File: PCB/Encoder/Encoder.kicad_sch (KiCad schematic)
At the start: 19 parts, among them J2 1-1734595-0, J3 Conn_01x06_Pin, U2 DS90LV017ATMX/NOPB, U3 AS5047P-ATSM, U4 DS90LV018ATM, U5 DS90LV018ATM

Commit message: Updated Schematics and PCB
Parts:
- removed C2, C4, C6: 0.001uF, symbol Device:C
- removed C3, C5, C7: 0.1uF, symbol Device:C
- removed C8: 4.7uF, symbol Device:C
- removed FB2, FB3: 600R, FerriteBeadCustom:IND_BOURNS_1005, symbol Device:FerriteBead
- removed J3: Conn_01x06_Pin, symbol Connector:Conn_01x06_Pin
- removed R1, R2: 100R, symbol Device:R
- removed U2: DS90LV017ATMX/NOPB, LVDSCustom:SOIC127P599X175-8N, symbol LVDSCustom:DS90LV017ATMX_NOPB
- removed U4, U5: DS90LV018ATM, DS90LV018ATM:SOIC127P599X175-8N, symbol LVDSCustom:DS90LV018ATM
- added H1, H2, H3, H4: MountingHole, MountingHole:MountingHole_3.2mm_M3, symbol Mechanical:MountingHole
- C1: footprint (none) -> Capacitor_SMD:C_0805_2012Metric
- C2: renamed from C9; footprint (none) -> Capacitor_SMD:C_0805_2012Metric
- J1: renamed from J2; value 1-1734595-0 -> 1-1734595-0 Header; footprint CON10_1X10_DUM_HPI_TYC -> ConnectorCustom:CON10_1X10_DUM_HPI_TYC
- U1: renamed from U3; footprint TSSOP14_OSM -> AngleSensor:TSSOP14_OSM
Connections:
- net CLK_M is gone; now on net I: J1.8
- net CLK_P is gone; now on net B: J1.7
- net MISO_M is gone; now on net A: J1.6
- net MISO_P is gone; now on net MOSI: J1.5
- net MOSI_M is gone; now on net CLK: J1.3
- net MOSI_P is gone; now on net CS_: J1.2
- net +3.3V: now also J1.1
- net CS_: no longer J1.4
- net MISO: now also J1.4
- net I: now reaches U1.14 (I/PWM)
- net A: now reaches U1.6 (B)
- net B: now reaches U1.7 (A)
- no-connect marks 10 -> 4
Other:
- note removed: "LVDS CMOS and Driver for Long Distance Signal Integrity"
- title: (none) -> Magnetic Angle Encoder

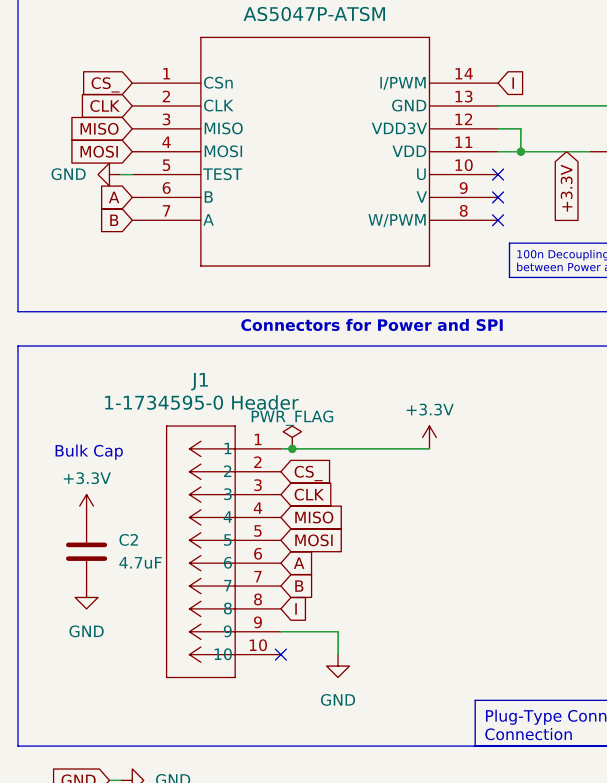
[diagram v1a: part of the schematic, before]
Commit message: Fixed GroundDetch not grounded
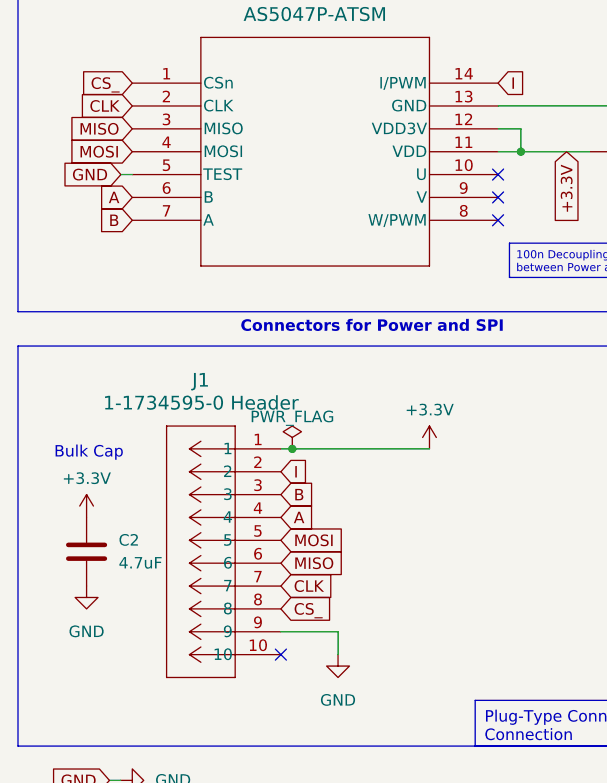
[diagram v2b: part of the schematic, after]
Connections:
- net A: now also J1.4; no longer J1.6
- net B: now also J1.3; no longer J1.7
- net CLK: now also J1.7; no longer J1.3
- net CS_: now also J1.8; no longer J1.2
- net GND: now also U1.5 (TEST)
- net I: now also J1.2; no longer J1.8
- net MISO: now also J1.6; no longer J1.4
